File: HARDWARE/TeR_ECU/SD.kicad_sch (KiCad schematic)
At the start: 7 parts, among them J3 Micro_SD_Card

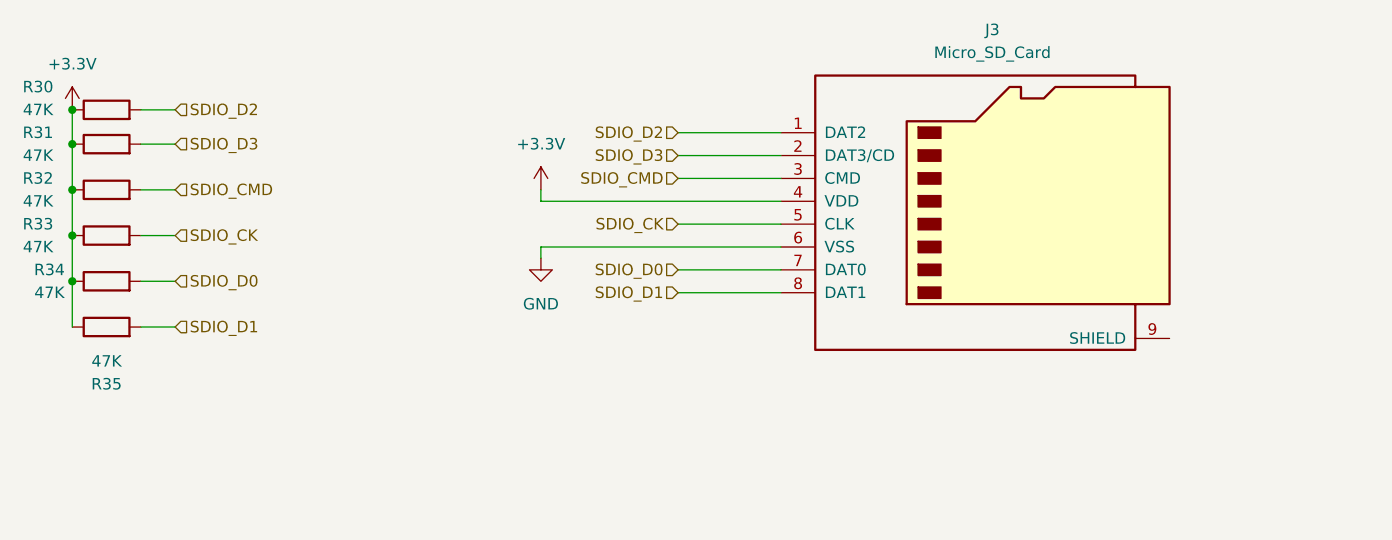
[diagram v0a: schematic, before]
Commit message: usb-c, good debug conn, switch
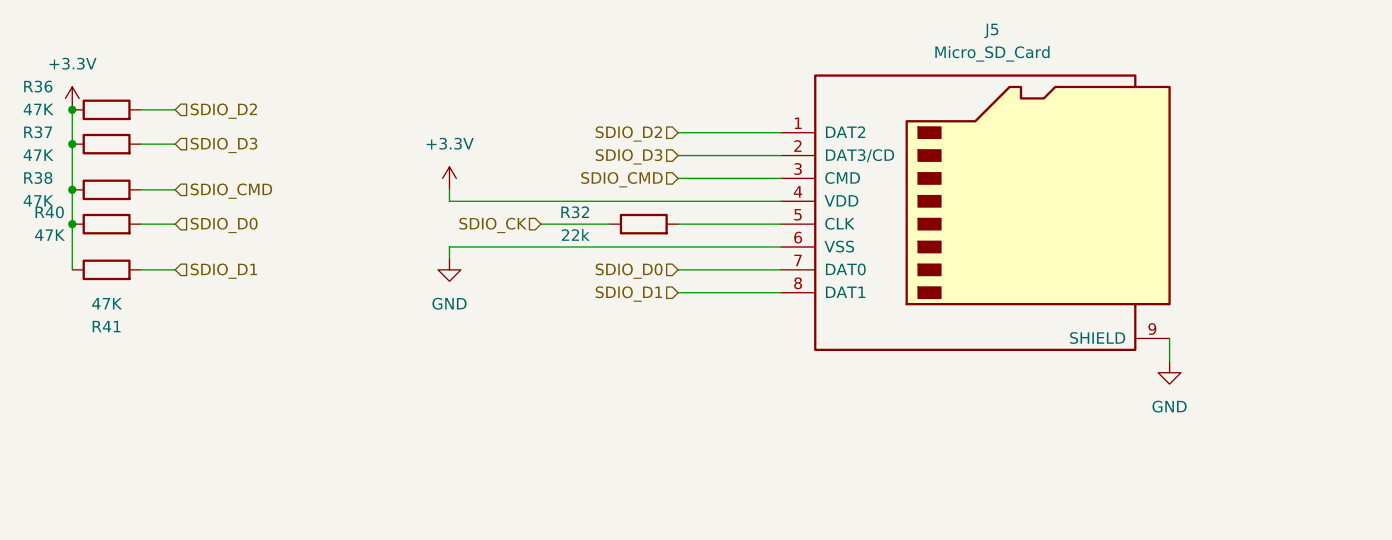
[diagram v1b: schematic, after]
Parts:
- removed R33: 47K, symbol Device:R
- added R32: 22k, symbol Device:R
- renumbered J3 to J5, R30 to R36, R31 to R37, R32 to R38, R34 to R40, R35 to R41
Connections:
- net GND: now also J5.9 (SHIELD)
- net SDIO_CK: now also R32.1; no longer J5.5 (CLK)
- new net: J5.5 (CLK), R32.2
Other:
- moved on the sheet: R40, R41

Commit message: Kept improving schmatic for V2
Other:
- moved on the sheet: J5, R32, R36, R37, R38, R40, R41

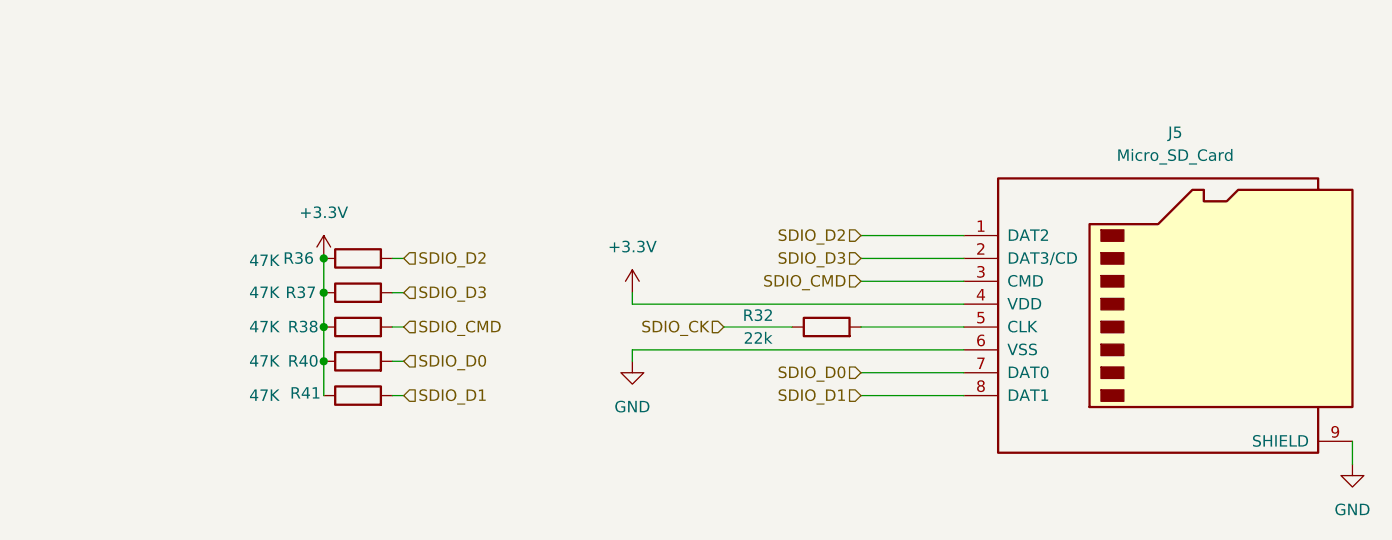
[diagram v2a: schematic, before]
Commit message: Advanced design and added IMU/GPS moduleç
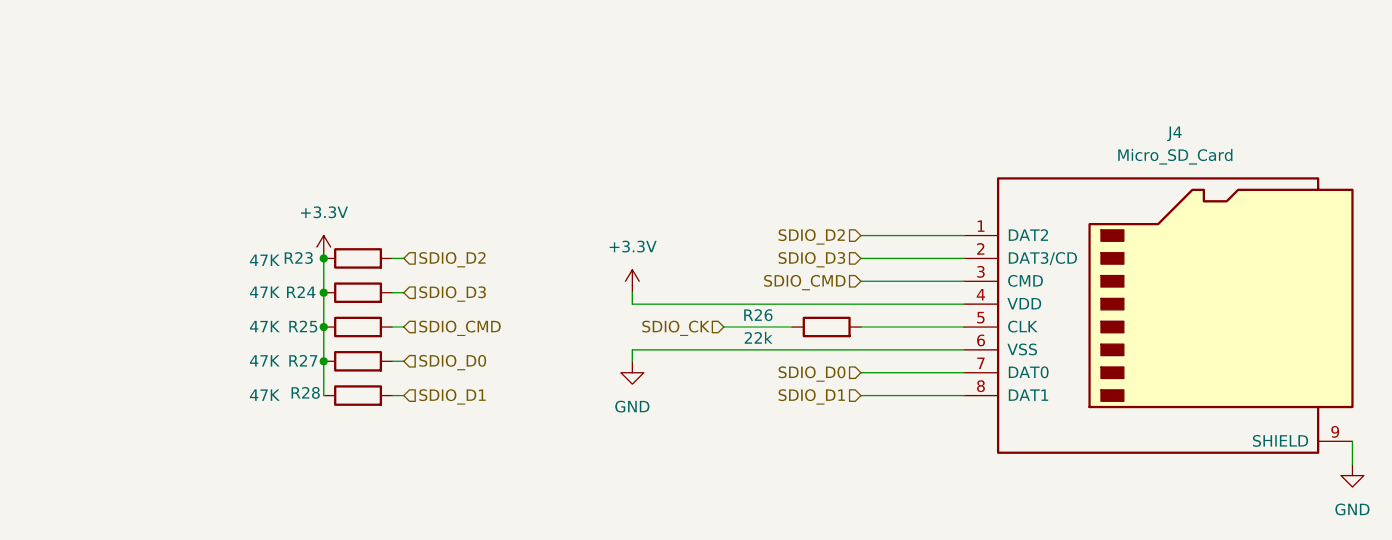
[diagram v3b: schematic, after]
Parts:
- renumbered J5 to J4, R36 to R23, R37 to R24, R38 to R25, R32 to R26, R40 to R27, R41 to R28
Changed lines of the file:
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@@
 		(on_board yes)
 		(dnp no)
-		(property "Reference" "R40"
+		(property "Reference" "R27"
 			(at 85.344 99.06 90)
 			(effects
@@
 			(project "TeR_ECU"
 				(path "/84413845-c4f3-4743-bcd2-a67649c90902/3e95f185-9df1-42f9-aa76-21fb32ee8ccb"
-					(reference "R40")
+					(reference "R27")
 					(unit 1)
 				)
@@
 		(dnp no)
 		(fields_autoplaced yes)
-		(property "Reference" "#PWR080"
+		(property "Reference" "#PWR073"
 			(at 87.63 91.44 0)
 			(effects
@@
 			(project "TeR_ECU"
 				(path "/84413845-c4f3-4743-bcd2-a67649c90902/3e95f185-9df1-42f9-aa76-21fb32ee8ccb"
-					(reference "#PWR080")
+					(reference "#PWR073")
 					(unit 1)
 				)
@@
 		(on_board yes)
 		(dnp no)
-		(property "Reference" "R41"
+		(property "Reference" "R28"
 			(at 85.598 102.616 90)
 			(effects
@@
 			(project "TeR_ECU"
 				(path "/84413845-c4f3-4743-bcd2-a67649c90902/3e95f185-9df1-42f9-aa76-21fb32ee8ccb"
-					(reference "R41")
+					(reference "R28")
 					(unit 1)
 				)
@@
 		(dnp no)
 		(fields_autoplaced yes)
-		(property "Reference" "J5"
+		(property "Reference" "J4"
 			(at 182.245 73.66 0)
 			(effects
@@
 			(project "TeR_ECU"
 				(path "/84413845-c4f3-4743-bcd2-a67649c90902/3e95f185-9df1-42f9-aa76-21fb32ee8ccb"
-					(reference "J5")
+					(reference "J4")
 					(unit 1)
 				)
@@
 		(dnp no)
 		(fields_autoplaced yes)
-		(property "Reference" "#PWR079"
+		(property "Reference" "#PWR075"
 			(at 121.92 105.41 0)
 			(effects
@@
 			(project "TeR_ECU"
 				(path "/84413845-c4f3-4743-bcd2-a67649c90902/3e95f185-9df1-42f9-aa76-21fb32ee8ccb"
-					(reference "#PWR079")
+					(reference "#PWR075")
 					(unit 1)
 				)
@@
 		(dnp no)
 		(fields_autoplaced yes)
-		(property "Reference" "#PWR081"
+		(property "Reference" "#PWR076"
 			(at 201.93 116.84 0)
 			(effects
@@
 			(project "TeR_ECU"
 				(path "/84413845-c4f3-4743-bcd2-a67649c90902/3e95f185-9df1-42f9-aa76-21fb32ee8ccb"
-					(reference "#PWR081")
+					(reference "#PWR076")
 					(unit 1)
 				)
@@
 		(on_board yes)
 		(dnp no)
-		(property "Reference" "R37"
+		(property "Reference" "R24"
 			(at 85.09 91.44 90)
 			(effects
@@
 			(project "TeR_ECU"
 				(path "/84413845-c4f3-4743-bcd2-a67649c90902/3e95f185-9df1-42f9-aa76-21fb32ee8ccb"
-					(reference "R37")
+					(reference "R24")
 					(unit 1)
 				)
@@
 		(on_board yes)
 		(dnp no)
-		(property "Reference" "R38"
+		(property "Reference" "R25"
 			(at 85.344 95.25 90)
 			(effects
@@
 			(project "TeR_ECU"
 				(path "/84413845-c4f3-4743-bcd2-a67649c90902/3e95f185-9df1-42f9-aa76-21fb32ee8ccb"
-					(reference "R38")
+					(reference "R25")
 					(unit 1)
 				)
@@
 		(on_board yes)
 		(dnp no)
-		(property "Reference" "R32"
+		(property "Reference" "R26"
 			(at 135.89 93.98 90)
 			(effects
@@
 			(project "TeR_ECU"
 				(path "/84413845-c4f3-4743-bcd2-a67649c90902/3e95f185-9df1-42f9-aa76-21fb32ee8ccb"
-					(reference "R32")
+					(reference "R26")
 					(unit 1)
 				)
@@
 		(dnp no)
 		(fields_autoplaced yes)
-		(property "Reference" "#PWR078"
+		(property "Reference" "#PWR074"
 			(at 121.92 95.25 0)
 			(effects
@@
 			(project "TeR_ECU"
 				(path "/84413845-c4f3-4743-bcd2-a67649c90902/3e95f185-9df1-42f9-aa76-21fb32ee8ccb"
-					(reference "#PWR078")
+					(reference "#PWR074")
 					(unit 1)
 				)
@@
 		(on_board yes)
 		(dnp no)
-		(property "Reference" "R36"
+		(property "Reference" "R23"
 			(at 84.836 87.63 90)
 			(effects
@@
 			(project "TeR_ECU"
 				(path "/84413845-c4f3-4743-bcd2-a67649c90902/3e95f185-9df1-42f9-aa76-21fb32ee8ccb"
-					(reference "R36")
-					(unit 1)
-				)
+					(reference "R23")
+					(unit 1)
+				)
